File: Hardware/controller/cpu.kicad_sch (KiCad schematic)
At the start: 36 parts, among them J301 Conn_ARM_JTAG_SWD_10, SW301 B3F-1005, U301 AT24CS32-SSHM, U302 ATSAME51J20A-A, Y301 32.768kHz, Y302 12MHz

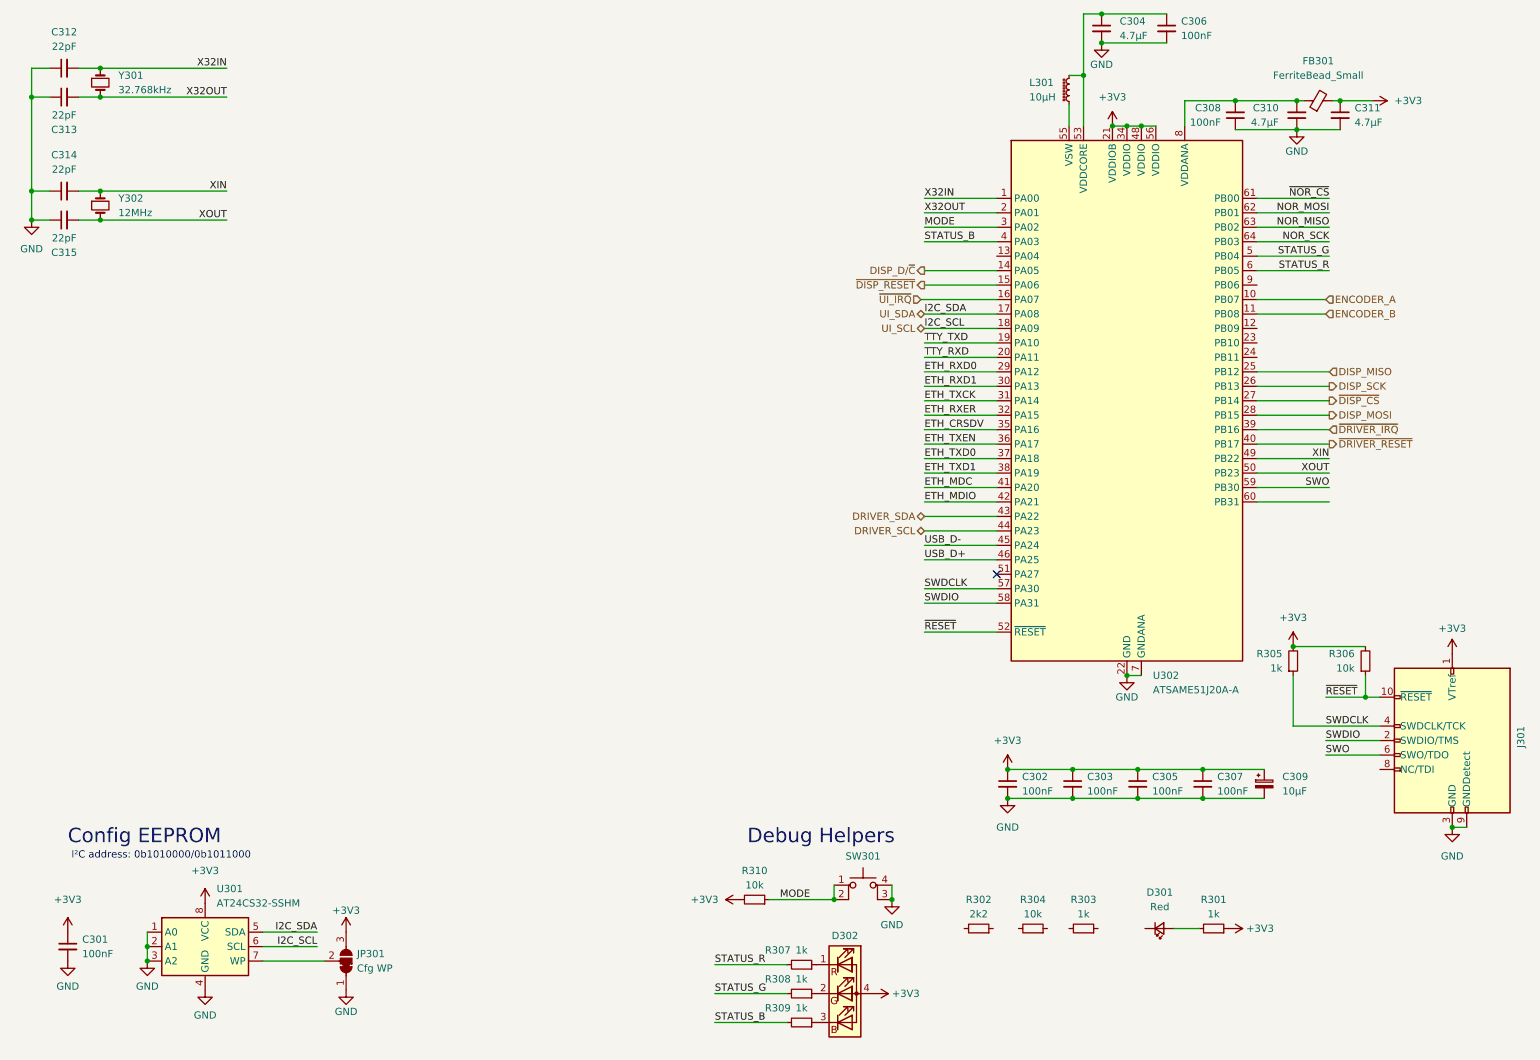
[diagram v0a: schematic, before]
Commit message: Basic controller board finished
- This just has the connections to the front panel and driver board; it
  lacks the rear IO connectors, a power button, and the Ethernet PHY
  currently
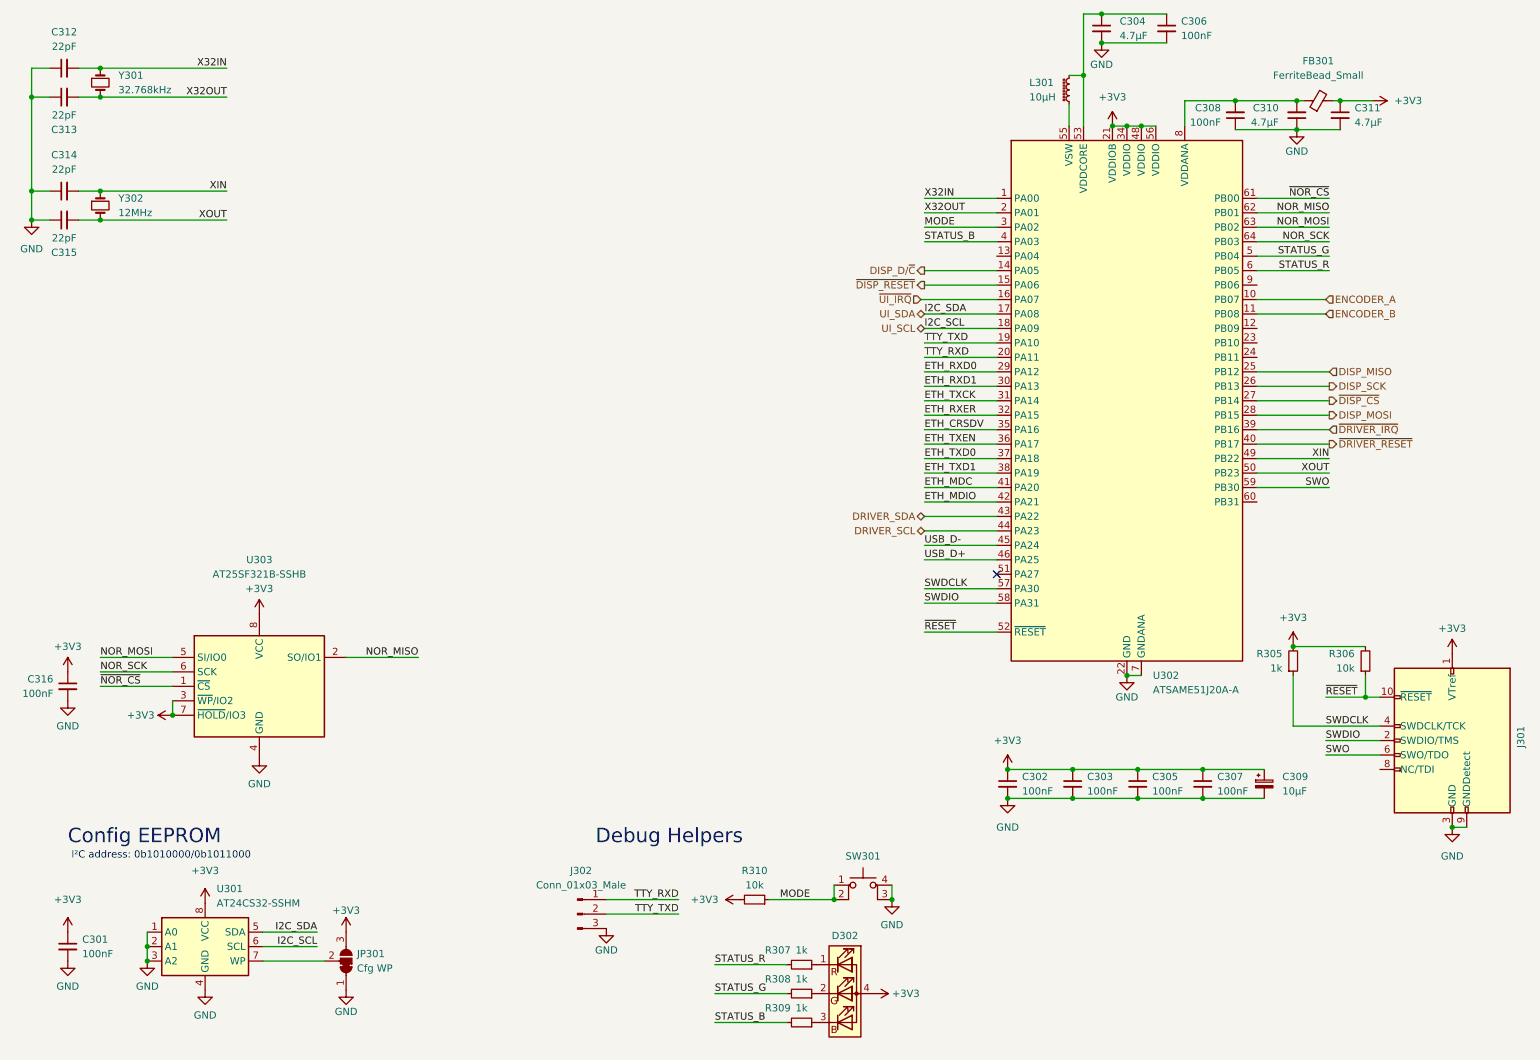
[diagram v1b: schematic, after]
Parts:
- removed D301: Red, LED_SMD:LED_0805_2012Metric_Pad1.15x1.40mm_HandSolder, symbol Device:LED_Small
- removed R301, R303: 1k, Resistor_SMD:R_0805_2012Metric_Pad1.20x1.40mm_HandSolder, symbol Device:R_Small
- removed R302: 2k2, Resistor_SMD:R_0805_2012Metric_Pad1.20x1.40mm_HandSolder, symbol Device:R_Small
- removed R304: 10k, Resistor_SMD:R_0805_2012Metric_Pad1.20x1.40mm_HandSolder, symbol Device:R_Small
- added C316: 100nF, Capacitor_SMD:C_0805_2012Metric_Pad1.18x1.45mm_HandSolder, symbol Device:C_Small
- added J302: Conn_01x03_Male, Connector_PinHeader_2.54mm:PinHeader_1x03_P2.54mm_Vertical, symbol Connector:Conn_01x03_Male
- added U303: AT25SF321B-SSHB, Package_SO:SOIC-8_3.9x4.9mm_P1.27mm, symbol programmable-load:AT25SF321B-SSHB
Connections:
- net +3V3: now also C316.1, U303.3 (~{WP}/IO2), U303.7 (~{HOLD}/IO3), U303.8 (VCC)
- net GND: now also C316.2, J302.3 (Pin_3), U303.4 (GND)
- net NOR_MISO: now also U302.62 (PB01), U303.2 (SO/IO1); no longer U302.63 (PB02)
- net NOR_MOSI: now also U302.63 (PB02), U303.5 (SI/IO0); no longer U302.62 (PB01)
- net NOR_SCK: now also U303.6 (SCK)
- net TTY_RXD: now also J302.1 (Pin_1)
- net TTY_TXD: now also J302.2 (Pin_2)
- net ~{NOR_CS}: now also U303.1 (~{CS})

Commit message: Added basic rear IO connector
- Placed the connector for the rear IO board, which will carry USB, I2C,
  Ethernet and power. Currently, USB and I2C have been hooked up.

- Added an I2C switch. This will allow sharing the secondary I2C bus
  between the front panel and rear IO, without needing to worry about
  address conflicts or other such issues.

  Removed the on-board I2C EEPROM; we have a NOR flash instead.
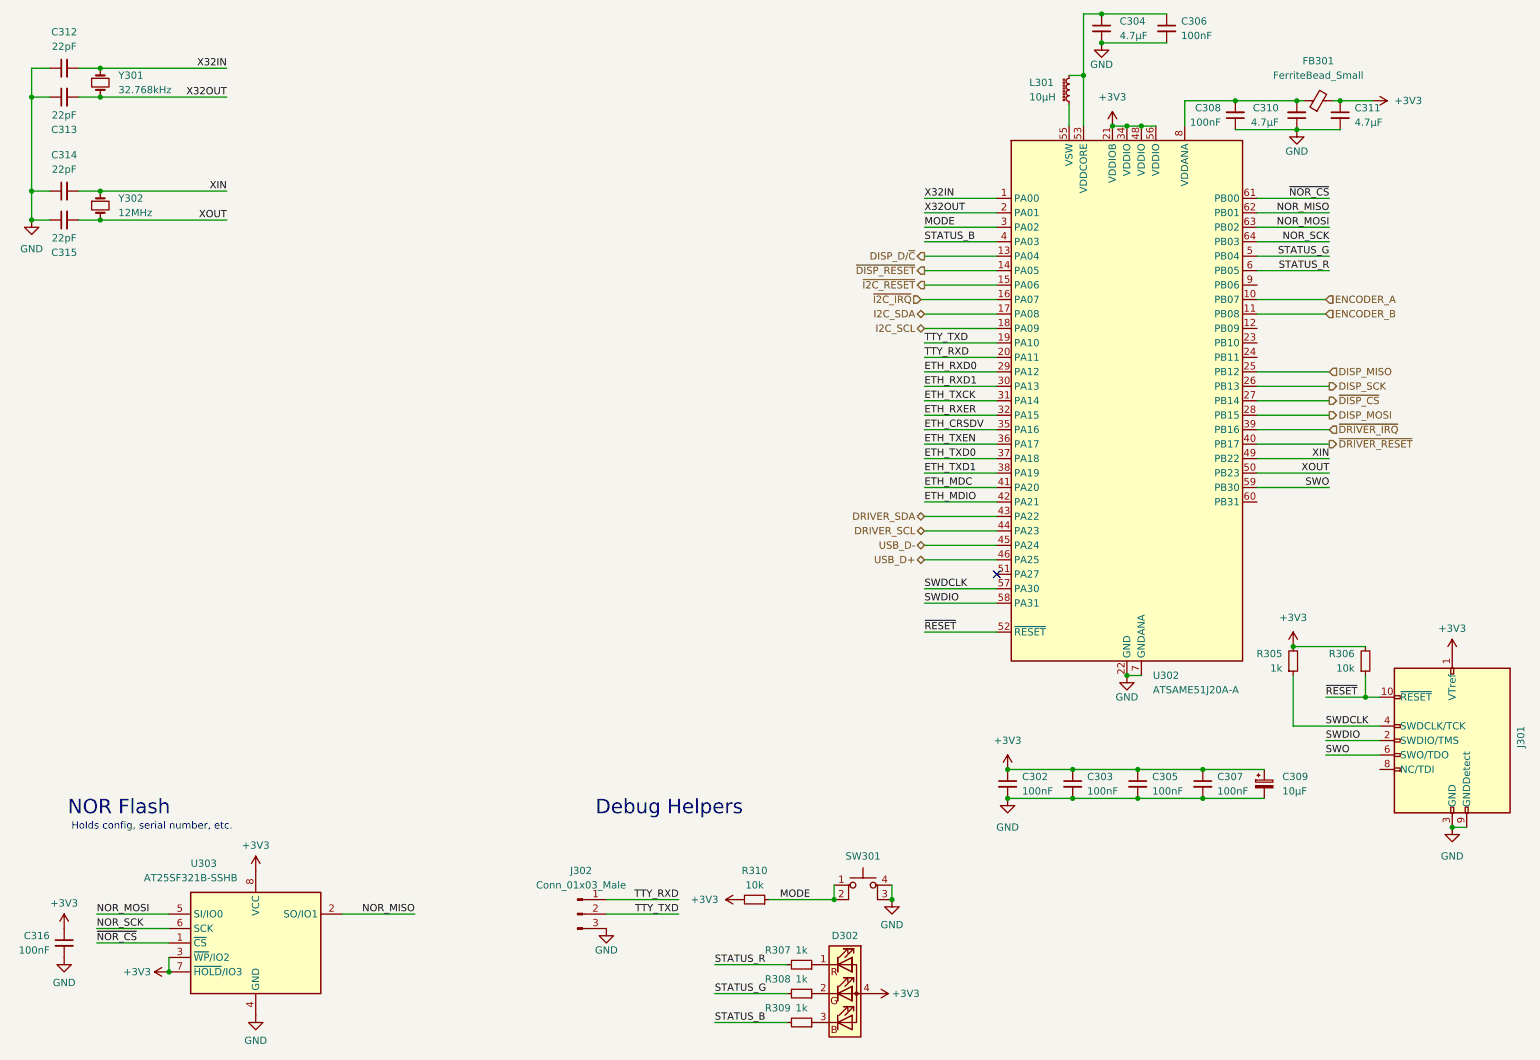
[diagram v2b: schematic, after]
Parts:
- removed C301: 100nF, Capacitor_SMD:C_0805_2012Metric_Pad1.18x1.45mm_HandSolder, symbol Device:C_Small
- removed JP301: Cfg WP, Connector_PinHeader_2.54mm:PinHeader_1x03_P2.54mm_Vertical, symbol Jumper:SolderJumper_3_Bridged12
- removed U301: AT24CS32-SSHM, Package_SO:SOIC-8_3.9x4.9mm_P1.27mm, symbol Memory_EEPROM:AT24CS32-SSHM
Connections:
- net DISP_D/~{C}: now also U302.13 (PA04); no longer U302.14 (PA05)
- net ~{DISP_RESET}: now also U302.14 (PA05); no longer U302.15 (PA06)
- net UI_SCL renamed I2C_SCL
- net UI_SDA renamed I2C_SDA
- net ~{UI_IRQ} renamed ~{I2C_IRQ}
- new net ~{I2C_RESET}: U302.15 (PA06)
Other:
- note added: "Holds config, serial number, etc."
- note added: "NOR Flash"
- note removed: "Config EEPROM"
- note removed: "I²C address: 0b1010000/0b1011000"
- moved on the sheet: C316, U303

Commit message: Added Ethernet PHY
- Placed the Ethernet PHY on the controller board, and routed its lines
  to the rear panel connector. The MAC address will be stored in the NOR
  flash, and will need to be programmed in. (This avoids the complexity
  of needing a larger I2C switch to give us another bus for an I2C
  EEPROM; though we could ostensibly put one on the rear IO board.)
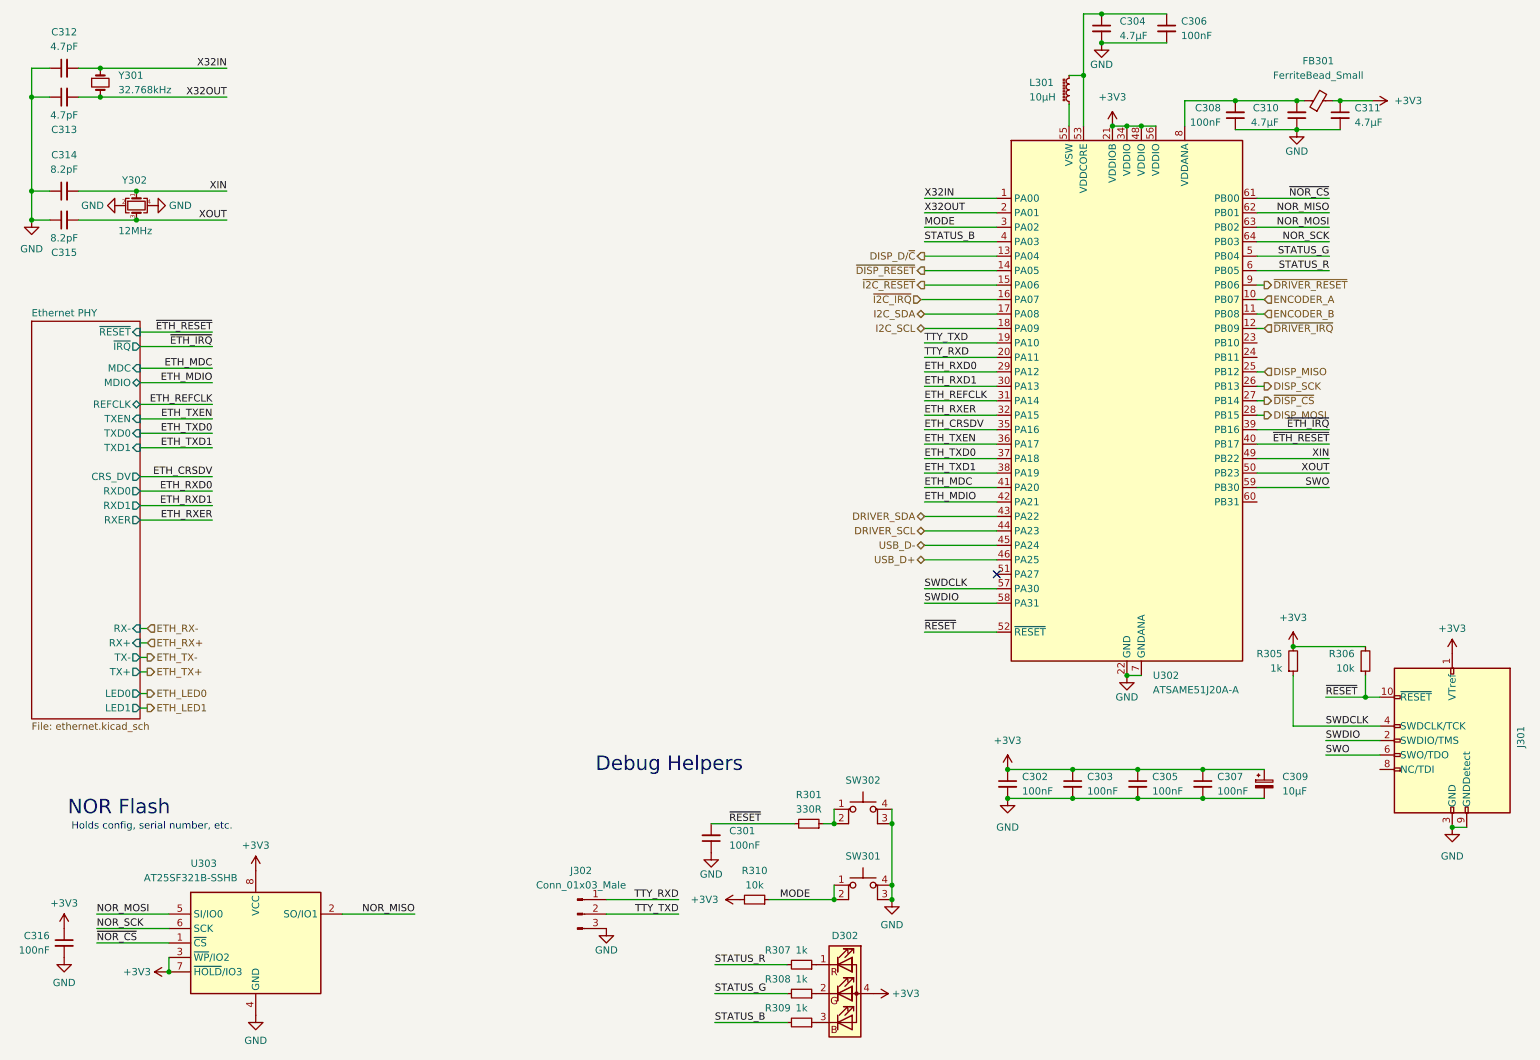
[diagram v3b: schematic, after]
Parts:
- added C301: 100nF, Capacitor_SMD:C_0805_2012Metric_Pad1.18x1.45mm_HandSolder, symbol Device:C_Small
- added R301: 330R, Resistor_SMD:R_0805_2012Metric_Pad1.20x1.40mm_HandSolder, symbol Device:R_Small
- added SW302: B3F-1002, Button_Switch_THT:SW_TH_Tactile_Omron_B3F-10xx, symbol Switch:SW_MEC_5E
- C312, C313: value 22pF -> 4.7pF; MPN CL21C220JBANFNC -> 0805N4R7C501CT
- C314, C315: value 22pF -> 8.2pF; MPN CL21C220JBANFNC -> 0805N8R2C500CT
- SW301: Color (none) -> Orange
- Y302: footprint Crystal:Crystal_SMD_ECS_CSM3X-2Pin_7.6x4.1mm -> Crystal:Crystal_SMD_3225-4Pin_3.2x2.5mm_HandSoldering; symbol Device:Crystal_Small -> Device:Crystal_GND24_Small; MPN ECS-120-20-3X-TR -> ECS-120-20-33-CKM-TR3
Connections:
- net GND: now also Y302.2, Y302.4, C301.1, SW302.3 (K), SW302.4 (A)
- net XOUT: now also Y302.3; no longer Y302.2
- net ~{DRIVER_IRQ}: now also U302.12 (PB09); no longer U302.39 (PB16)
- net ~{DRIVER_RESET}: now also U302.9 (PB06); no longer U302.40 (PB17)
- net ~{RESET}: now also C301.2, R301.2
- net ETH_TXCK renamed ETH_REFCLK
- new net: R301.1, SW302.1, SW302.2
- new net ~{ETH_IRQ}: U302.39 (PB16)
- new net ~{ETH_RESET}: U302.40 (PB17)
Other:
- added sheet Ethernet PHY (ethernet.kicad_sch)
- title: (none) -> Processor Complex
